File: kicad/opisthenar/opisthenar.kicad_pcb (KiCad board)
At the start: 2 copper layers, 41.9 x 42.5 mm, 11 parts, among them J5 CONN_01X14, J6 CONN_01X14, U1 ATMEGA328P-PU, Y1 16MHz Crystal

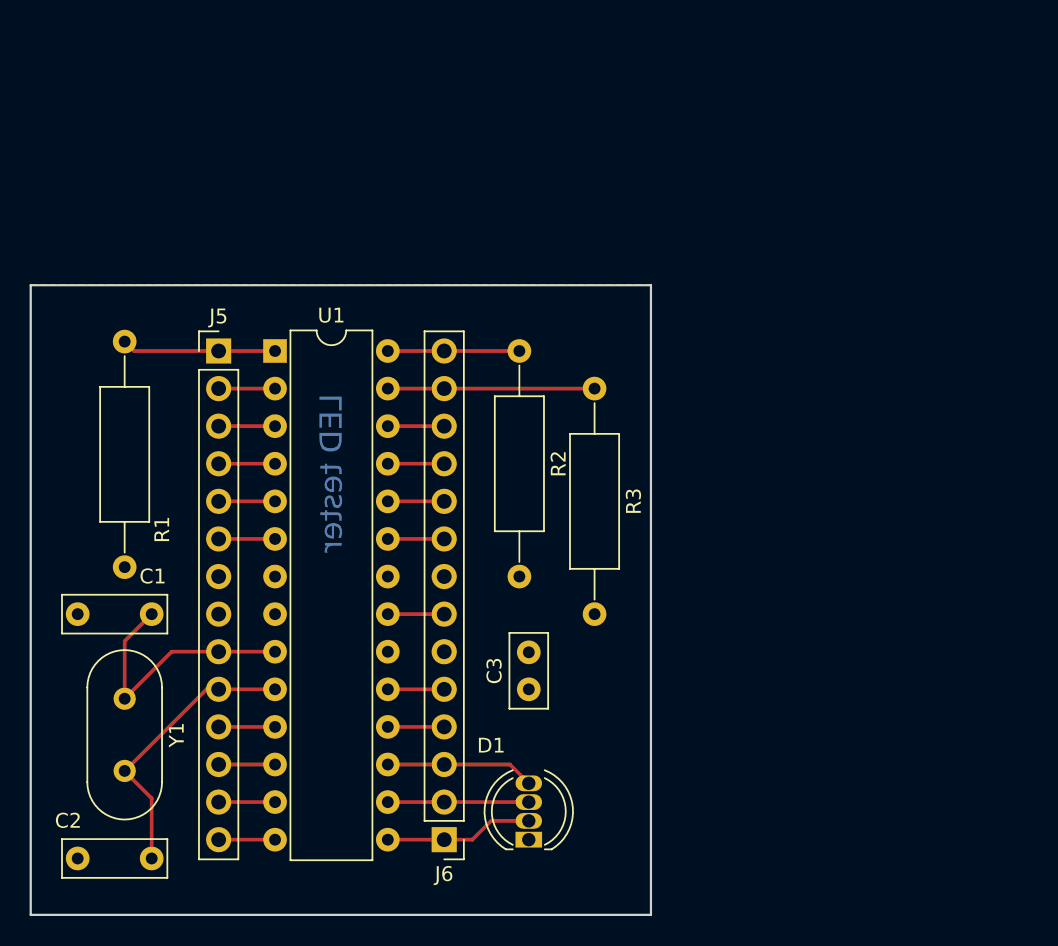
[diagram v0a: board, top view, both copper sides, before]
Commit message: Added TCA to kicad schmatic
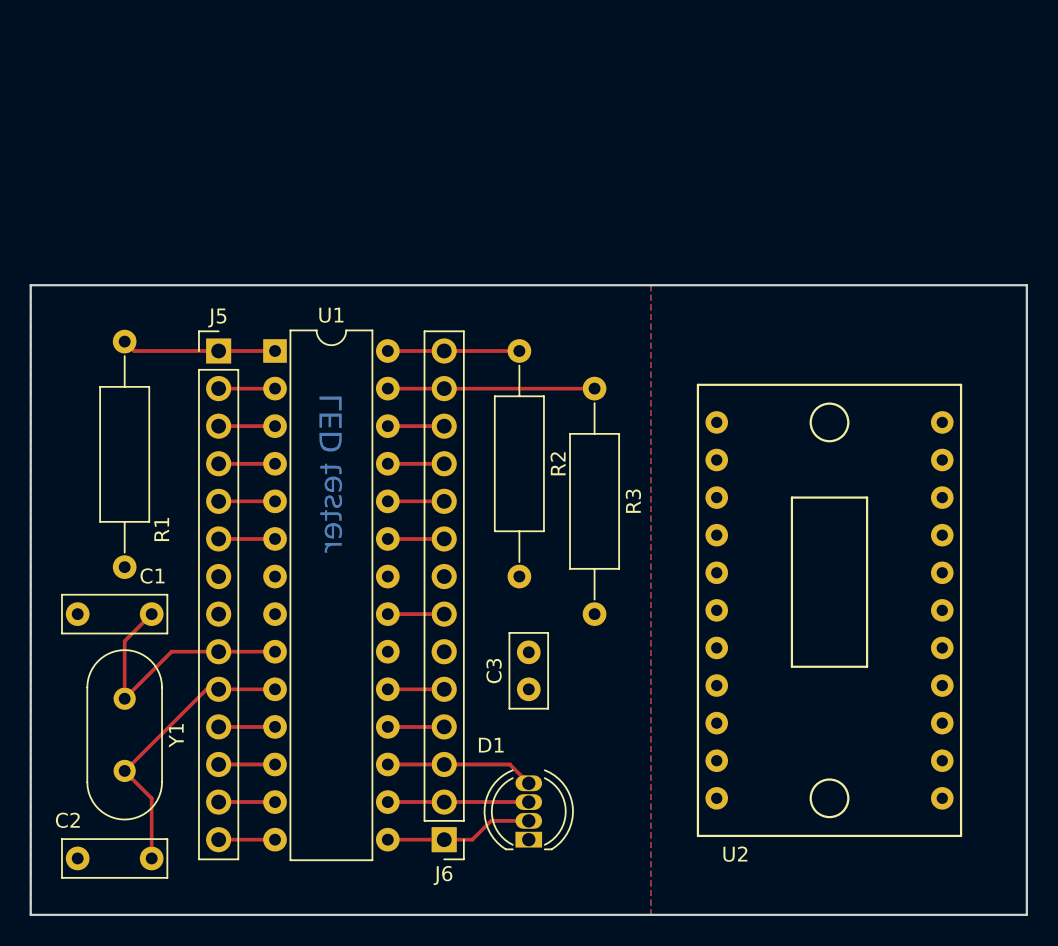
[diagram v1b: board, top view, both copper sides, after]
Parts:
- added U2: TCA9548A_ADAFRUIT, opisthenar:TCA9548A_ADAFRUIT, F.Cu at (153.7, 75.9)
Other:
- board size 41.9 x 42.5 mm -> 67.3 x 42.5 mm
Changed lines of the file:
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@@
     (tracks 42)
     (zones 0)
-    (modules 11)
-    (nets 27)
+    (modules 12)
+    (nets 49)
   )
   (page A4)
   (layers
     (0 F.Cu signal hide)
-    (31 B.Cu signal)
+    (31 B.Cu signal hide)
     (32 B.Adhes user)
     (33 F.Adhes user)
@@
   (net 25 /PC2)
   (net 26 /PC3)
+  (net 27 "Net-(U2-Pad1)")
+  (net 28 "Net-(U2-Pad3)")
+  (net 29 "Net-(U2-Pad4)")
+  (net 30 "Net-(U2-Pad5)")
+  (net 31 "Net-(U2-Pad6)")
+  (net 32 "Net-(U2-Pad7)")
+  (net 33 "Net-(U2-Pad8)")
+  (net 34 "Net-(U2-Pad9)")
+  (net 35 "Net-(U2-Pad10)")
+  (net 36 "Net-(U2-Pad11)")
+  (net 37 "Net-(U2-Pad12)")
+  (net 38 "Net-(U2-Pad13)")
+  (net 39 "Net-(U2-Pad14)")
+  (net 40 "Net-(U2-Pad15)")
+  (net 41 "Net-(U2-Pad16)")
+  (net 42 "Net-(U2-Pad17)")
+  (net 43 "Net-(U2-Pad18)")
+  (net 44 "Net-(U2-Pad19)")
+  (net 45 "Net-(U2-Pad20)")
+  (net 46 "Net-(U2-Pad21)")
+  (net 47 "Net-(U2-Pad22)")
+  (net 48 "Net-(U2-Pad23)")
   (net_class Default "This is the default net class."
     (clearance 0.2)
@@
     (add_net /~RESET)
     (add_net GND)
+    (add_net "Net-(U2-Pad1)")
+    (add_net "Net-(U2-Pad10)")
+    (add_net "Net-(U2-Pad11)")
+    (add_net "Net-(U2-Pad12)")
+    (add_net "Net-(U2-Pad13)")
+    (add_net "Net-(U2-Pad14)")
+    (add_net "Net-(U2-Pad15)")
+    (add_net "Net-(U2-Pad16)")
+    (add_net "Net-(U2-Pad17)")
+    (add_net "Net-(U2-Pad18)")
+    (add_net "Net-(U2-Pad19)")
+    (add_net "Net-(U2-Pad20)")
+    (add_net "Net-(U2-Pad21)")
+    (add_net "Net-(U2-Pad22)")
+    (add_net "Net-(U2-Pad23)")
+    (add_net "Net-(U2-Pad3)")
+    (add_net "Net-(U2-Pad4)")
+    (add_net "Net-(U2-Pad5)")
+    (add_net "Net-(U2-Pad6)")
+    (add_net "Net-(U2-Pad7)")
+    (add_net "Net-(U2-Pad8)")
+    (add_net "Net-(U2-Pad9)")
     (add_net VCC)
   )
@@
     )
   )
+  (module opisthenar:TCA9548A_ADAFRUIT (layer F.Cu)
+    (at 153.67 75.946)
+    (fp_text reference U2 (at 2.54 31.75) (layer F.SilkS)
+      (effects (font (size 1 1) (thickness 0.15)))
+    )
+    (fp_text value TCA9548A_ADAFRUIT (at 7.62 -1.27) (layer F.Fab)
+      (effects (font (size 1 1) (thickness 0.15)))
+    )
+    (fp_line (start 6.35 7.62) (end 11.43 7.62) (layer F.SilkS) (width 0.15))
+    (fp_line (start 11.43 7.62) (end 11.43 19.05) (layer F.SilkS) (width 0.15))
+    (fp_line (start 11.43 19.05) (end 6.35 19.05) (layer F.SilkS) (width 0.15))
+    (fp_line (start 6.35 19.05) (end 6.35 7.62) (layer F.SilkS) (width 0.15))
+    (fp_circle (center 8.89 27.94) (end 10.16 27.94) (layer F.SilkS) (width 0.15))
+    (fp_circle (center 8.89 2.54) (end 10.16 2.54) (layer F.SilkS) (width 0.15))
+    (fp_line (start 0 30.48) (end 17.78 30.48) (layer F.SilkS) (width 0.15))
+    (fp_line (start 17.78 30.48) (end 17.78 0) (layer F.SilkS) (width 0.15))
+    (fp_line (start 17.78 0) (end 0 0) (layer F.SilkS) (width 0.15))
+    (fp_line (start 0 0) (end 0 30.48) (layer F.SilkS) (width 0.15))
+    (pad 1 thru_hole circle (at 1.27 2.54) (size 1.524 1.524) (drill 0.762) (layers *.Cu *.Mask)
+      (net 27 "Net-(U2-Pad1)"))
+    (pad 3 thru_hole circle (at 1.27 5.08) (size 1.524 1.524) (drill 0.762) (layers *.Cu *.Mask)
+      (net 28 "Net-(U2-Pad3)"))
+    (pad 4 thru_hole circle (at 1.27 7.62) (size 1.524 1.524) (drill 0.762) (layers *.Cu *.Mask)
+      (net 29 "Net-(U2-Pad4)"))
+    (pad 5 thru_hole circle (at 1.27 10.16) (size 1.524 1.524) (drill 0.762) (layers *.Cu *.Mask)
+      (net 30 "Net-(U2-Pad5)"))
+    (pad 6 thru_hole circle (at 1.27 12.7) (size 1.524 1.524) (drill 0.762) (layers *.Cu *.Mask)
+      (net 31 "Net-(U2-Pad6)"))
+    (pad 7 thru_hole circle (at 1.27 15.24) (size 1.524 1.524) (drill 0.762) (layers *.Cu *.Mask)
+      (net 32 "Net-(U2-Pad7)"))
+    (pad 8 thru_hole circle (at 1.27 17.78) (size 1.524 1.524) (drill 0.762) (layers *.Cu *.Mask)
+      (net 33 "Net-(U2-Pad8)"))
+    (pad 9 thru_hole circle (at 1.27 20.32) (size 1.524 1.524) (drill 0.762) (layers *.Cu *.Mask)
+      (net 34 "Net-(U2-Pad9)"))
+    (pad 10 thru_hole circle (at 1.27 22.86) (size 1.524 1.524) (drill 0.762) (layers *.Cu *.Mask)
+      (net 35 "Net-(U2-Pad10)"))
+    (pad 11 thru_hole circle (at 1.27 25.4) (size 1.524 1.524) (drill 0.762) (layers *.Cu *.Mask)
+      (net 36 "Net-(U2-Pad11)"))
+    (pad 12 thru_hole circle (at 1.27 27.94) (size 1.524 1.524) (drill 0.762) (layers *.Cu *.Mask)
+      (net 37 "Net-(U2-Pad12)"))
+    (pad 13 thru_hole circle (at 16.51 27.94) (size 1.524 1.524) (drill 0.762) (layers *.Cu *.Mask)
+      (net 38 "Net-(U2-Pad13)"))
+    (pad 14 thru_hole circle (at 16.51 25.4) (size 1.524 1.524) (drill 0.762) (layers *.Cu *.Mask)
+      (net 39 "Net-(U2-Pad14)"))
+    (pad 15 thru_hole circle (at 16.51 22.86) (size 1.524 1.524) (drill 0.762) (layers *.Cu *.Mask)
+      (net 40 "Net-(U2-Pad15)"))
+    (pad 16 thru_hole circle (at 16.51 20.32) (size 1.524 1.524) (drill 0.762) (layers *.Cu *.Mask)
+      (net 41 "Net-(U2-Pad16)"))
+    (pad 17 thru_hole circle (at 16.51 17.78) (size 1.524 1.524) (drill 0.762) (layers *.Cu *.Mask)
+      (net 42 "Net-(U2-Pad17)"))
+    (pad 18 thru_hole circle (at 16.51 15.24) (size 1.524 1.524) (drill 0.762) (layers *.Cu *.Mask)
+      (net 43 "Net-(U2-Pad18)"))
+    (pad 19 thru_hole circle (at 16.51 12.7) (size 1.524 1.524) (drill 0.762) (layers *.Cu *.Mask)
+      (net 44 "Net-(U2-Pad19)"))
+    (pad 20 thru_hole circle (at 16.51 10.16) (size 1.524 1.524) (drill 0.762) (layers *.Cu *.Mask)
+      (net 45 "Net-(U2-Pad20)"))
+    (pad 21 thru_hole circle (at 16.51 7.62) (size 1.524 1.524) (drill 0.762) (layers *.Cu *.Mask)
+      (net 46 "Net-(U2-Pad21)"))
+    (pad 22 thru_hole circle (at 16.51 5.08) (size 1.524 1.524) (drill 0.762) (layers *.Cu *.Mask)
+      (net 47 "Net-(U2-Pad22)"))
+    (pad 23 thru_hole circle (at 16.51 2.54) (size 1.524 1.524) (drill 0.762) (layers *.Cu *.Mask)
+      (net 48 "Net-(U2-Pad23)"))
+  )
   (gr_text "LED Tester" (at 111.125 76.835 90) (layer B.SilkS)
     (effects (font (size 1.5 1.5) (thickness 0.3)) (justify mirror))
@@
   )
   (gr_line (start 108.585 69.215) (end 108.585 111.76) (angle 90) (layer Edge.Cuts) (width 0.15))
-  (gr_line (start 150.495 69.215) (end 108.585 69.215) (angle 90) (layer Edge.Cuts) (width 0.15))
-  (gr_line (start 150.495 111.76) (end 150.495 69.215) (angle 90) (layer Edge.Cuts) (width 0.15))
-  (gr_line (start 108.585 111.76) (end 150.495 111.76) (angle 90) (layer Edge.Cuts) (width 0.15))
+  (gr_line (start 175.895 69.215) (end 108.585 69.215) (angle 90) (layer Edge.Cuts) (width 0.15))
+  (gr_line (start 175.895 111.76) (end 175.895 69.215) (angle 90) (layer Edge.Cuts) (width 0.15))
+  (gr_line (start 108.585 111.76) (end 175.895 111.76) (angle 90) (layer Edge.Cuts) (width 0.15))
   (segment (start 114.935 97.155) (end 114.935 93.265) (width 0.25) (layer F.Cu) (net 2))
   (segment (start 114.935 93.265) (end 116.76 91.44) (width 0.25) (layer F.Cu) (net 2))

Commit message: Updated opisthenar pcb for new pcb run.
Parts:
- removed R2, R3: 4.7K, Resistors_ThroughHole:R_Axial_DIN0309_L9.0mm_D3.2mm_P15.24mm_Horizontal
- added G***: LOGO, kicad:logo, B.Cu at (161.8, 92.2)
- added J1: CONN_01X12, Pin_Headers:Pin_Header_Straight_1x12_Pitch2.54mm, F.Cu at (150.4, 79.0)
- added J2: CONN_01X12, Pin_Headers:Pin_Header_Straight_1x12_Pitch2.54mm, F.Cu at (173.0, 106.9)
- added J3: CONN_01X07, Pin_Headers:Pin_Header_Straight_1x07_Pitch2.54mm, F.Cu at (145.5, 74.9)
- added J4: CONN_01X07, Pin_Headers:Pin_Header_Straight_1x07_Pitch2.54mm, F.Cu at (141.5, 74.9)
- added U3: ESP-01v090, ESP8266:ESP-01, F.Cu at (158.0, 74.9)
- added wifi_led1: LED, LEDs:LED_D3.0mm, F.Cu at (145.5, 96.3)
- moved U2 1.93 mm to (152.9, 77.7)
- moved C3 1.30 mm to (141.0, 96.3), turned to 270 degrees
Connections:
- U2 pad 1: Net-(U2-Pad1) -> VCC
- U2 pad 10: Net-(U2-Pad10) -> /SC0
- U2 pad 11: Net-(U2-Pad11) -> /SD1
- U2 pad 12: Net-(U2-Pad12) -> /SC1
- U2 pad 13: Net-(U2-Pad13) -> /SD2
- U2 pad 14: Net-(U2-Pad14) -> /SC2
- U2 pad 15: Net-(U2-Pad15) -> /SD3
- U2 pad 16: Net-(U2-Pad16) -> /SC3
- U2 pad 17: Net-(U2-Pad17) -> /SD4
- U2 pad 18: Net-(U2-Pad18) -> /SC4
- U2 pad 19: Net-(U2-Pad19) -> /SD5
- U2 pad 20: Net-(U2-Pad20) -> /SC5
- U2 pad 21: Net-(U2-Pad21) -> /SD6
- U2 pad 22: Net-(U2-Pad22) -> /SC6
- U2 pad 23: Net-(U2-Pad23) -> /SD7
- U2 pad 3: Net-(U2-Pad3) -> /SDA
- U2 pad 4: Net-(U2-Pad4) -> /SCL
- U2 pad 5: Net-(U2-Pad5) -> /~TCA_RESET
- U2 pad 6: Net-(U2-Pad6) -> /TCA_A0
- U2 pad 7: Net-(U2-Pad7) -> /TCA_A1
- U2 pad 8: Net-(U2-Pad8) -> /TCA_A2
- U2 pad 9: Net-(U2-Pad9) -> /SD0
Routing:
- net /TX: track 3.81 -> 60.1 mm, vias 0 -> 1
- net Net-(U3-Pad4): track 0.00 -> 43.2 mm
- net /~RESET: track 10.4 -> 51.5 mm, vias 0 -> 1
- net /RX: track 3.81 -> 43.5 mm, vias 0 -> 1
- net /SCL: track 8.89 -> 44.7 mm, vias 0 -> 1
- net /SDA: track 14.0 -> 44.1 mm
- net /~TCA_RESET: track 0.00 -> 3.81 mm
- net /TCA_A2: track 0.00 -> 3.81 mm
- net /TCA_A1: track 0.00 -> 3.81 mm
- net /TCA_A0: track 0.00 -> 3.81 mm
- net /SD1: track 0.00 -> 3.81 mm
- net /SD0: track 0.00 -> 3.81 mm
- net /SC1: track 0.00 -> 3.81 mm
- net /SC0: track 0.00 -> 3.81 mm
- net /SD7: track 0.00 -> 3.56 mm
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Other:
- board text added: "Opisthenar v0"
- board text removed: "LED Tester"
- board text removed: "LED tester"
